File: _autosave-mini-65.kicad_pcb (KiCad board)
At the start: 2 copper layers, 302.2 x 93.5 mm, 171 parts, among them J1 TYPE-C-31-M12_13_EDITED, J2 AVR-ISP-6, SW1 SW_Push, U1 ATmega32U4-AU, U2 USBLC6-2SC6, Y1 Crystal_GND24_Small

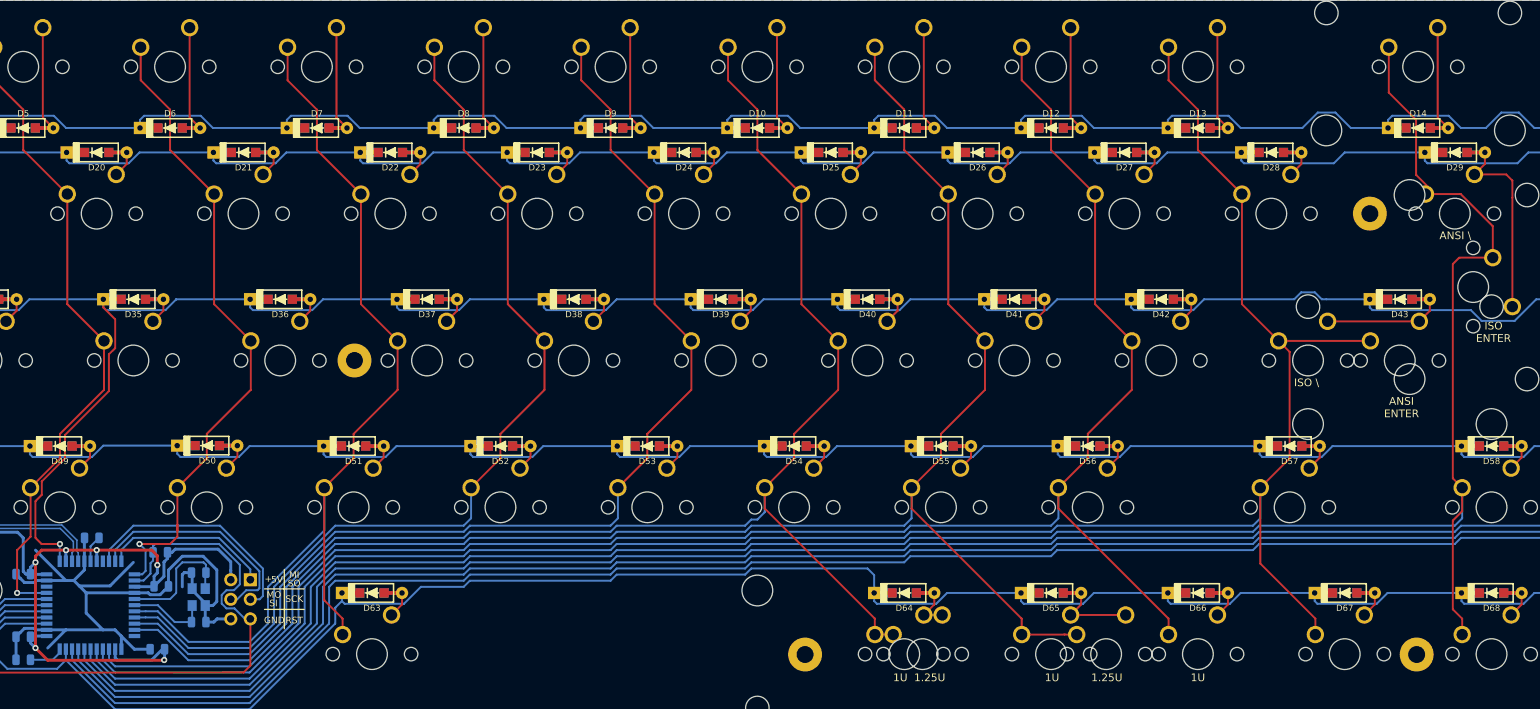
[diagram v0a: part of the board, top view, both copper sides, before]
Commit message: renamed diodes starting at 0
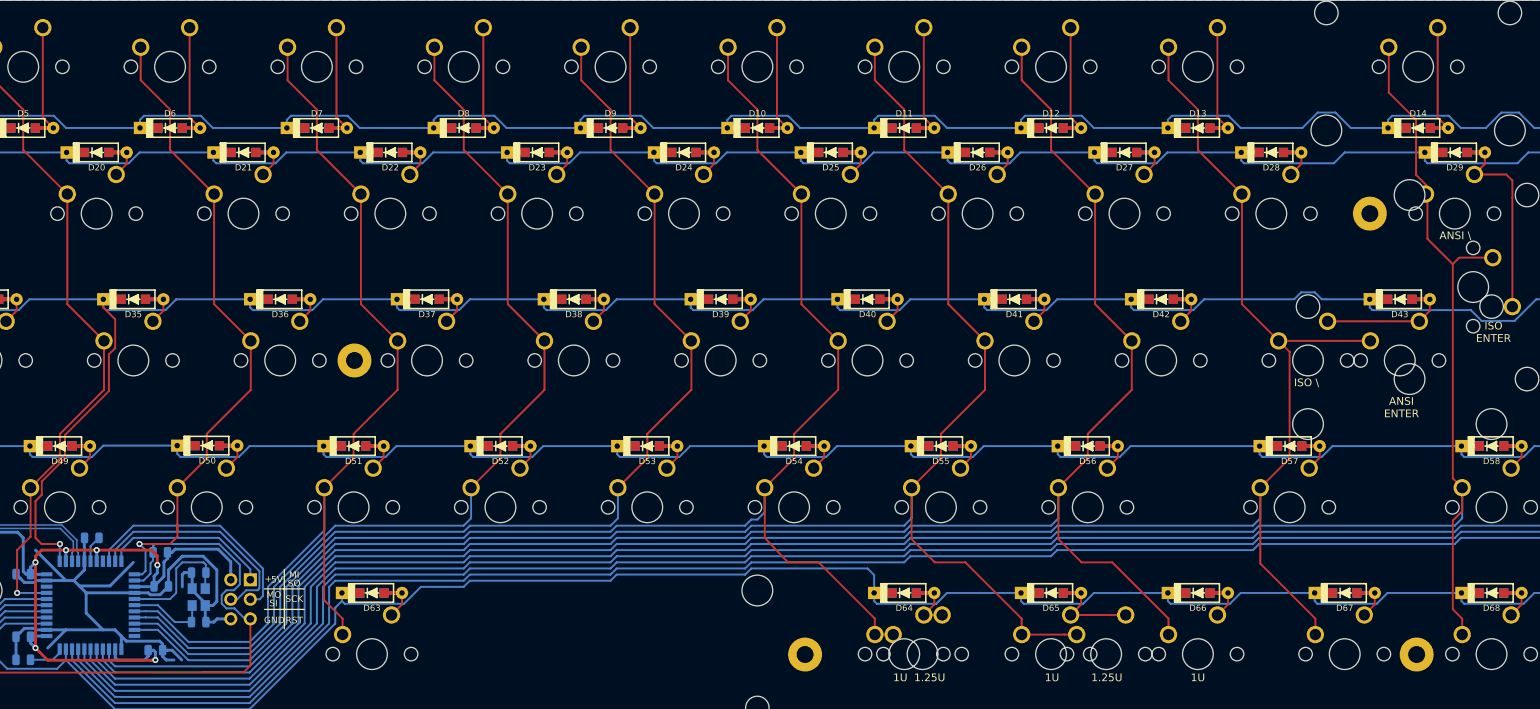
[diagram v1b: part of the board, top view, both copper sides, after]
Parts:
- moved C5 0.28 mm to (23.5, 164.6), turned to 0 degrees
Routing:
- net GND: track 145.9 -> 153.5 mm
- net COL13: track 286.9 -> 283.1 mm
- net COL11: track 233.1 -> 235.4 mm
- net COL10: track 220.0 -> 222.3 mm
- net COL9: track 191.7 -> 194.0 mm
- net +5V: track 235.4 -> 233.1 mm
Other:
- rule pad_to_mask_clearance: 0.051 -> 0
- rule solder_mask_min_width: 0.25 -> 0.12
- rule trace_min: 0.2 -> 0.127
- rule via_min_size: 0.4 -> 0.6
